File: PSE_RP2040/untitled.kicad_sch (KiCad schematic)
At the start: 28 parts

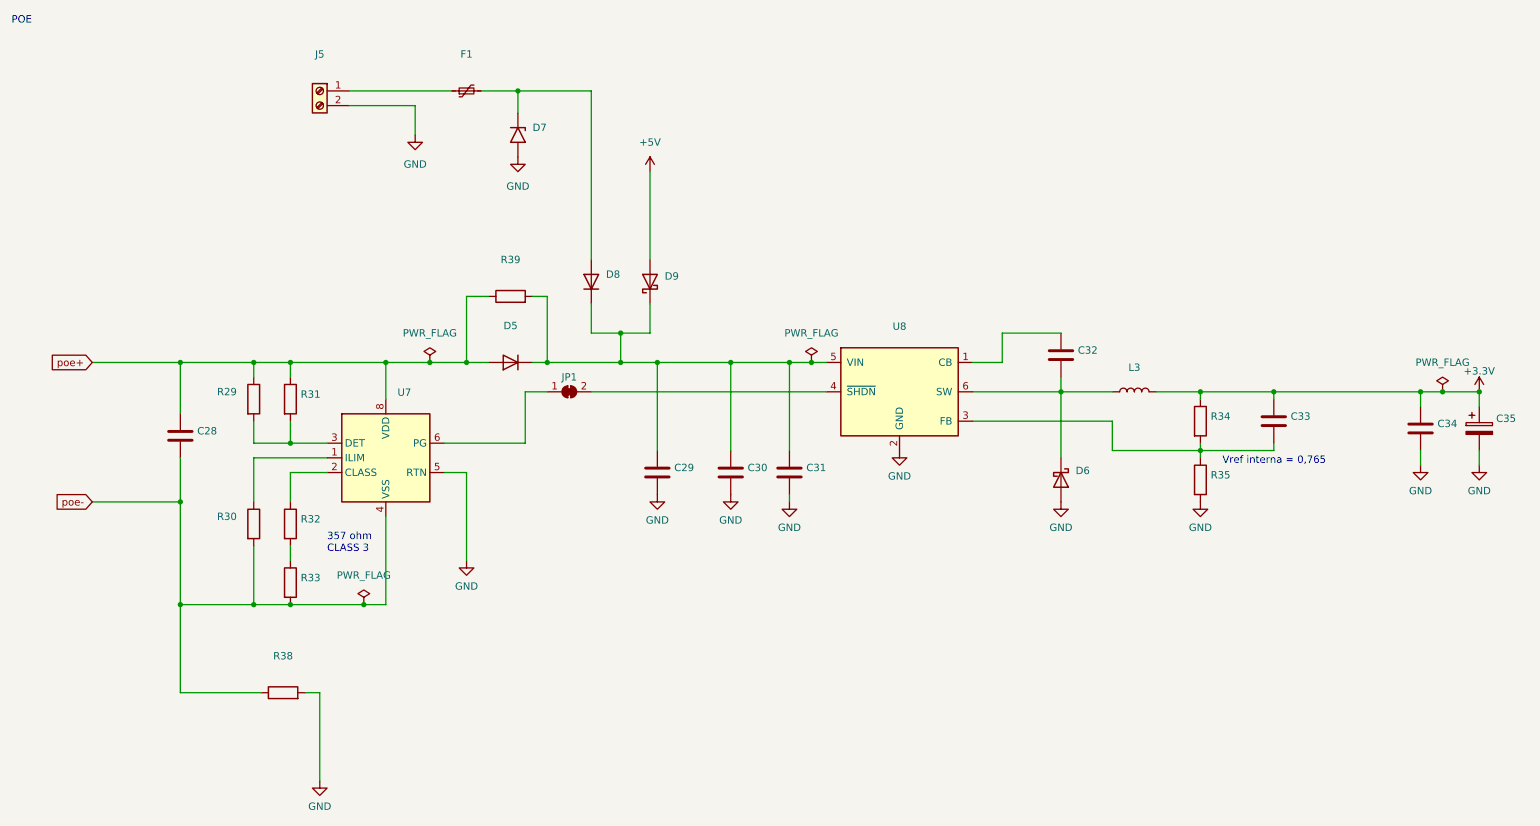
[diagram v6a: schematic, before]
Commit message: PCB
Aggiunto strato rame bottom, tolto mounting hole 4 dallo schematico, aggiunti fiducial (solo sul PCB), riduzione margine scheda, sbroglio.
(larghezza max piste in uscita dal micro 7 mils)
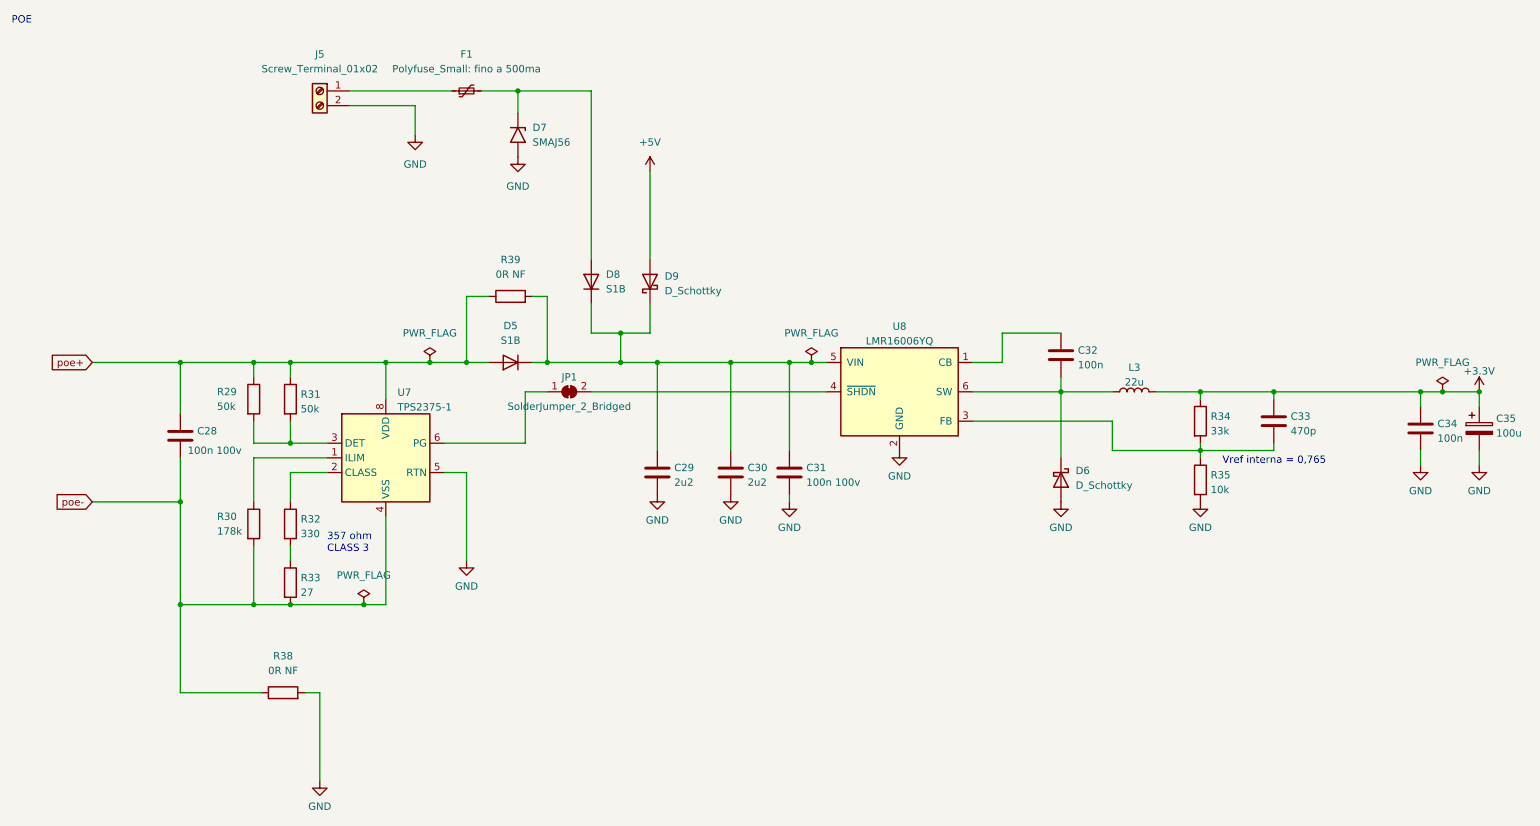
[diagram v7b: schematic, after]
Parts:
- C28, C31: value (none) -> 100n 100v; footprint (none) -> Capacitor_SMD:C_0603_1608Metric
- C29, C30: value (none) -> 2u2; footprint (none) -> Capacitor_SMD:C_0603_1608Metric
- C32, C34: value (none) -> 100n; footprint (none) -> Capacitor_SMD:C_0603_1608Metric
- C33: value (none) -> 470p; footprint (none) -> Capacitor_SMD:C_0603_1608Metric
- C35: value (none) -> 100u; footprint (none) -> Capacitor_SMD:C_0805_2012Metric
- D5, D8: value (none) -> S1B; footprint (none) -> Diode_SMD:D_SMA
- D6, D9: value (none) -> D_Schottky; footprint (none) -> Diode_SMD:D_SMA
- D7: value (none) -> SMAJ56; footprint (none) -> Diode_SMD:D_SMA
- F1: value (none) -> Polyfuse_Small: fino a 500ma; footprint (none) -> Fuse:Fuse_1812_4532Metric
- J5: value (none) -> Screw_Terminal_01x02; footprint (none) -> TerminalBlock_Phoenix:TerminalBlock_Phoenix_MKDS-1,5-2-5.08_1x02_P5.08mm_Horizontal
- JP1: value (none) -> SolderJumper_2_Bridged; footprint (none) -> Jumper:SolderJumper-2_P1.3mm_Bridged_Pad1.0x1.5mm
- L3: value (none) -> 22u; footprint (none) -> Inductor_SMD:L_Vishay_IFSC-1515AH_4x4x1.8mm
- R29, R31: value (none) -> 50k; footprint (none) -> Resistor_SMD:R_0603_1608Metric
- R30: value (none) -> 178k; footprint (none) -> Resistor_SMD:R_0603_1608Metric
- R32: value (none) -> 330; footprint (none) -> Resistor_SMD:R_0603_1608Metric
- R33: value (none) -> 27; footprint (none) -> Resistor_SMD:R_0603_1608Metric
- R34: value (none) -> 33k; footprint (none) -> Resistor_SMD:R_0603_1608Metric
- R35: value (none) -> 10k; footprint (none) -> Resistor_SMD:R_0603_1608Metric
- R38, R39: value (none) -> 0R NF; footprint (none) -> Resistor_SMD:R_0603_1608Metric
- U7: value (none) -> TPS2375-1; footprint (none) -> Package_SO:SOIC-8_5.275x5.275mm_P1.27mm
- U8: value (none) -> LMR16006YQ; footprint (none) -> Package_TO_SOT_SMD:SOT-23-6

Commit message: Gerber controllati
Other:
- title: (none) -> PPSE_LAN_NTP
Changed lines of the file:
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@@
 (kicad_sch (version 20211123) (generator eeschema)
   (paper "A4")
+  (title_block
+    (title "PPSE_LAN_NTP")
+    (date "2022-04-12")
+    (rev "0")
+  )
   (junction (at 95.25 74.93) (diameter 0) (color 0 0 0 0)
   )
